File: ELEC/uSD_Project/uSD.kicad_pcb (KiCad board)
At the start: 2 copper layers, 70.6 x 25.3 mm, 18 parts, among them J1 CONN_01X08, J2 CONN_01X08, J3 CONN_02X04, J4 CONN_02X04, J5 CONN_01X08, J6 CONN_01X08, J7 CONN_01X20, U1 74HC595, U2 74HC165, U3 PADI_IoT_Stamp

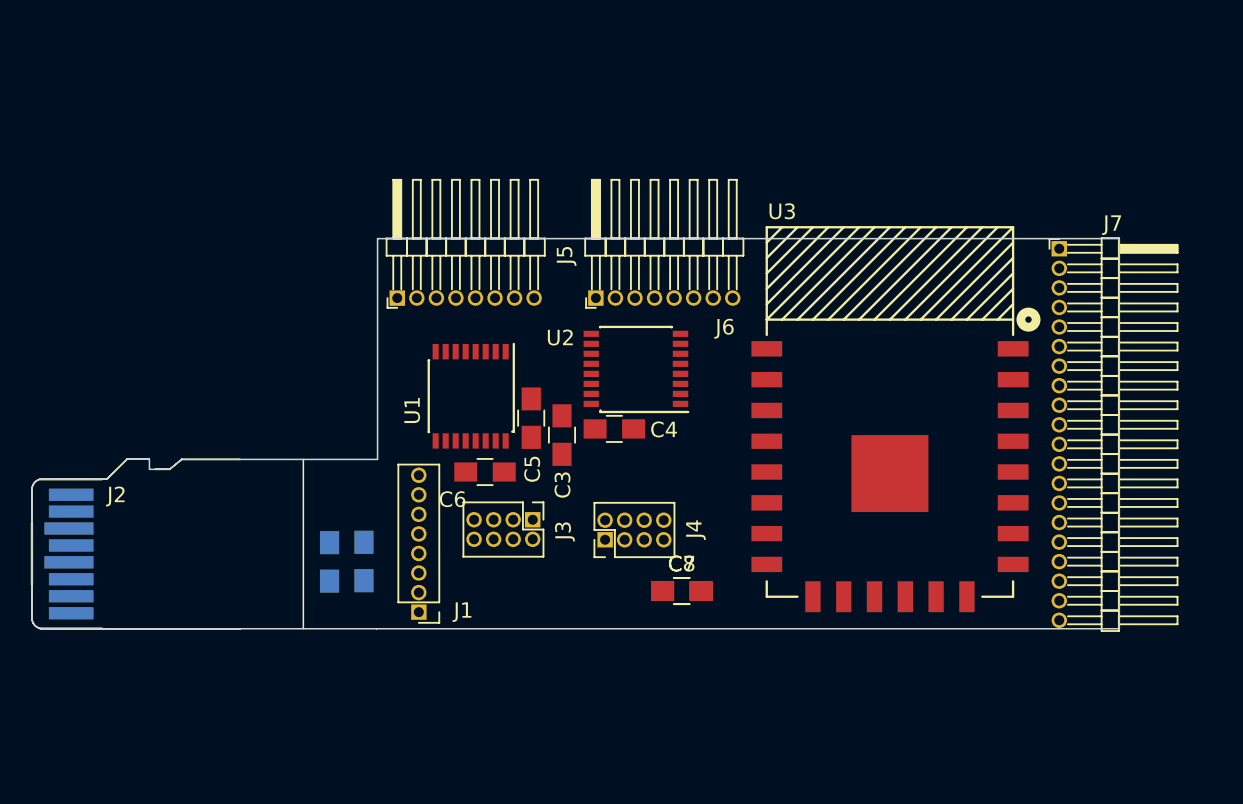
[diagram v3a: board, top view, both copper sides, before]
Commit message: Changed out shift registers, started and almost completed routing
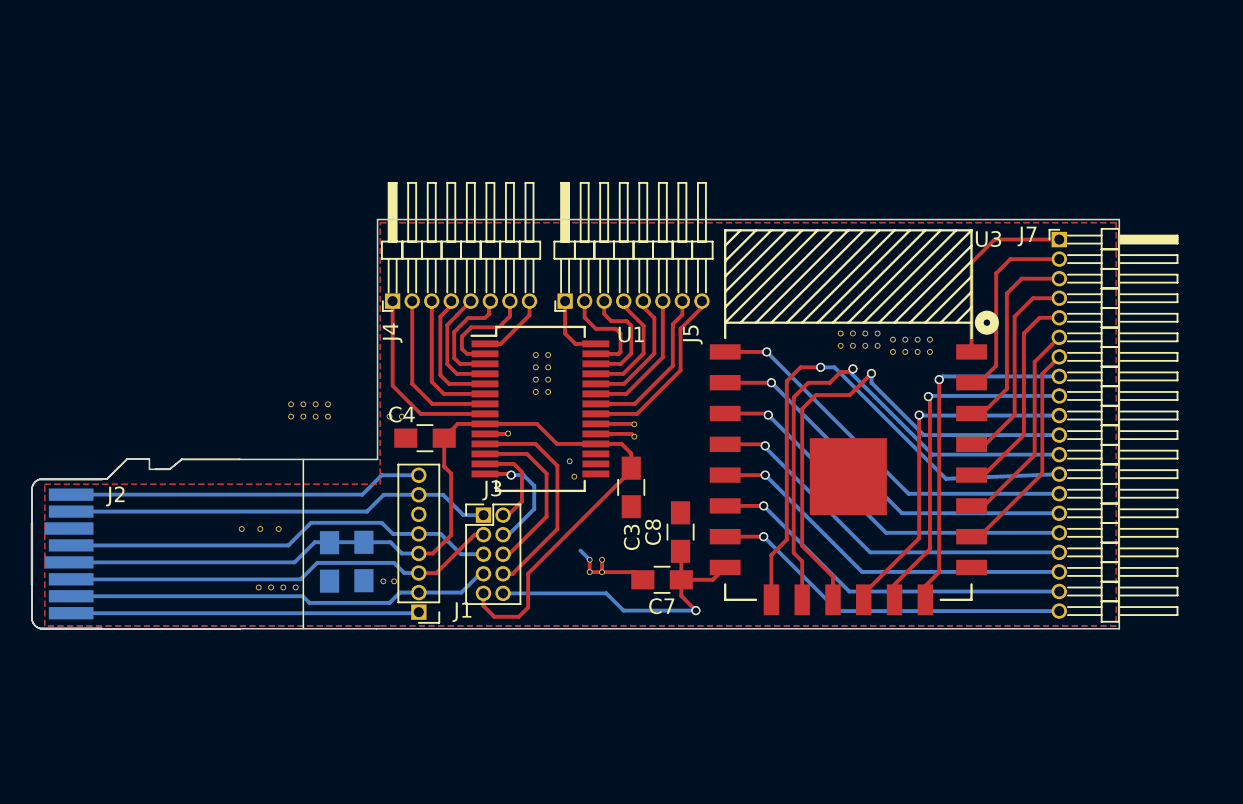
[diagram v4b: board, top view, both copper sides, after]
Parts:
- removed C5: 100nF, Capacitors_SMD:C_0805_HandSoldering
- removed C6: 1uF, Capacitors_SMD:C_0805_HandSoldering
- removed U2: 74HC165, Housings_SSOP.pretty:SSOP-16_4.4x5.2mm_Pitch0.65mm
- added J8: CONN_01X01, Via:10mil_Via, F.Cu at (153.5, 99.8)
- added REF**: Vias, Via:10mil_Via, F.Cu at (166.9, 93.9)
- added REF**: Vias, Via:10mil_Via, F.Cu at (171.1, 94.3)
- added REF**: Vias, Via:10mil_Via, F.Cu at (171.1, 95.1)
- added REF**: Vias, Via:10mil_Via, F.Cu at (170.3, 95.1)
- added REF**: Vias, Via:10mil_Via, F.Cu at (171.9, 95.1)
- added REF**: Vias, Via:10mil_Via, F.Cu at (172.7, 95.1)
- added REF**: Vias, Via:10mil_Via, F.Cu at (172.7, 94.3)
- added REF**: Vias, Via:10mil_Via, F.Cu at (171.9, 94.3)
- added REF**: Vias, Via:10mil_Via, F.Cu at (147.9, 95.3)
- added REF**: Vias, Via:10mil_Via, F.Cu at (147.9, 96.1)
- added REF**: Vias, Via:10mil_Via, F.Cu at (147.1, 96.1)
- added REF**: Vias, Via:10mil_Via, F.Cu at (167.7, 93.9)
- added REF**: Vias, Via:10mil_Via, F.Cu at (147.1, 95.3)
- added REF**: Vias, Via:10mil_Via, F.Cu at (147.1, 96.9)
- added REF**: Vias, Via:10mil_Via, F.Cu at (147.1, 97.7)
- added REF**: Vias, Via:10mil_Via, F.Cu at (147.9, 97.7)
- added REF**: Vias, Via:10mil_Via, F.Cu at (147.9, 96.9)
- added REF**: Vias, Via:10mil_Via, F.Cu at (132.8, 98.5)
- added REF**: Vias, Via:10mil_Via, F.Cu at (133.6, 98.5)
- added REF**: Vias, Via:10mil_Via, F.Cu at (133.6, 99.3)
- added REF**: Vias, Via:10mil_Via, F.Cu at (132.8, 99.3)
- added REF**: Vias, Via:10mil_Via, F.Cu at (131.2, 99.3)
- added REF**: Vias, Via:10mil_Via, F.Cu at (167.7, 94.7)
- added REF**: Vias, Via:10mil_Via, F.Cu at (132.0, 99.3)
- added REF**: Vias, Via:10mil_Via, F.Cu at (132.0, 98.5)
- added REF**: Vias, Via:10mil_Via, F.Cu at (131.2, 98.5)
- added REF**: Vias, Via:10mil_Via, F.Cu at (138.4, 99.3)
- added REF**: Vias, Via:10mil_Via, F.Cu at (137.6, 99.3)
- added REF**: Vias, Via:10mil_Via, F.Cu at (145.3, 100.4)
- added REF**: Vias, Via:10mil_Via, F.Cu at (149.3, 102.2)
- added REF**: Vias, Via:10mil_Via, F.Cu at (149.6, 103.2)
- added REF**: Vias, Via:10mil_Via, F.Cu at (137.2, 110.0)
- added REF**: Vias, Via:10mil_Via, F.Cu at (137.9, 110.0)
- added REF**: Vias, Via:10mil_Via, F.Cu at (166.9, 94.7)
- added REF**: Vias, Via:10mil_Via, F.Cu at (131.5, 110.4)
- added REF**: Vias, Via:10mil_Via, F.Cu at (130.7, 110.4)
- added REF**: Vias, Via:10mil_Via, F.Cu at (129.1, 110.4)
- added REF**: Vias, Via:10mil_Via, F.Cu at (129.9, 110.4)
- added REF**: Vias, Via:10mil_Via, F.Cu at (128.0, 106.6)
- added REF**: Vias, Via:10mil_Via, F.Cu at (129.2, 106.6)
- added REF**: Vias, Via:10mil_Via, F.Cu at (130.4, 106.6)
- added REF**: Vias, Via:10mil_Via, F.Cu at (151.4, 109.4)
- added REF**: Vias, Via:10mil_Via, F.Cu at (151.4, 108.6)
- added REF**: Vias, Via:10mil_Via, F.Cu at (150.6, 108.6)
- added REF**: Vias, Via:10mil_Via, F.Cu at (168.5, 94.7)
- added REF**: Vias, Via:10mil_Via, F.Cu at (150.6, 109.4)
- added REF**: Vias, Via:10mil_Via, F.Cu at (169.3, 94.7)
- added REF**: Vias, Via:10mil_Via, F.Cu at (169.3, 93.9)
- added REF**: Vias, Via:10mil_Via, F.Cu at (168.5, 93.9)
- added REF**: Vias, Via:10mil_Via, F.Cu at (170.3, 94.3)
- C3: value 100nF -> 1uF
- J3: value CONN_02X04 -> CONN_02X05; footprint Pin_Headers:Pin_Header_Straight_2x04_Pitch1.27mm -> Pin_Headers:Pin_Header_Straight_2x05_Pitch1.27mm
- J4: value CONN_02X04 -> CONN_01X08; footprint Pin_Headers:Pin_Header_Straight_2x04_Pitch1.27mm -> Pin_Headers:Pin_Header_Angled_1x08_Pitch1.27mm
- J6: value CONN_01X08 -> CONN_01X01; footprint Pin_Headers:Pin_Header_Angled_1x08_Pitch1.27mm -> Via:10mil_Via
- U1: value 74HC595 -> MCP23S17; footprint Housings_SSOP.pretty:SSOP-16_4.4x5.2mm_Pitch0.65mm -> Housings_SSOP.pretty:SSOP-28_5.3x10.2mm_Pitch0.65mm
- moved J4 20.8 mm to (137.8, 91.8)
- moved C4 12.3 mm to (139.9, 100.7), turned to 180 degrees
- moved J5 10.9 mm to (149.0, 91.8)
- moved J6 9.34 mm to (153.5, 100.6)
- moved C3 5.64 mm to (153.3, 103.9)
- moved U1 4.60 mm to (147.4, 98.8), turned to 0 degrees
- moved C8 3.83 mm to (156.5, 106.8), turned to 90 degrees
- moved J3 3.21 mm to (143.7, 105.7), turned to 0 degrees
- moved U3 2.71 mm to (159.4, 111.2)
- moved C7 1.48 mm to (155.3, 109.9), turned to 180 degrees
- moved J7 0.60 mm to (181.1, 87.8)
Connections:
- C1 pad 1: VCC -> VDD
- C2 pad 1: VCC -> VDD
- C3 pad 1: VCC -> VDD
- C4 pad 1: VCC -> VDD
- C7 pad 1: /Vdd_WIFI -> /Vdd_Wifi
- C8 pad 1: /Vdd_WIFI -> /Vdd_Wifi
- J1 pad 4: VCC -> VDD
- J2 pad 5: VCC -> VDD
- J3 pad 1: /595_Dat -> /DO
- J3 pad 2: /DO -> /MCP_DO
- J3 pad 3: /595_SRCLK -> /DI
- J3 pad 4: /CLK -> /MCP_DI
- J3 pad 5: /595_/OE -> /CLK
- J3 pad 6: /NC -> /MCP_CLK
- J3 pad 7: Net-(J3-Pad7) -> //CS
- J3 pad 8: Net-(J3-Pad8) -> /MCP_/CS
- J4 pad 1: /DI -> Net-(J4-Pad1)
- J4 pad 2: /165_Dat -> Net-(J4-Pad2)
- J4 pad 3: /CLK -> Net-(J4-Pad3)
- J4 pad 4: /165_CLK -> Net-(J4-Pad4)
- J4 pad 5: //CS -> Net-(J4-Pad5)
- J4 pad 6: /165_SHLD -> Net-(J4-Pad6)
- J4 pad 7: VCC -> Net-(J4-Pad7)
- J4 pad 8: /Vdd_WIFI -> Net-(J4-Pad8)
- J5 pad 1: /595_QH -> Net-(J5-Pad1)
- J5 pad 2: /595_QG -> Net-(J5-Pad2)
- J5 pad 3: /595_QF -> Net-(J5-Pad3)
- J5 pad 4: /595_QE -> Net-(J5-Pad4)
- J5 pad 5: /595_QD -> Net-(J5-Pad5)
- J5 pad 6: /595_QC -> Net-(J5-Pad6)
- J5 pad 7: /595_QB -> Net-(J5-Pad7)
- J5 pad 8: /595_QA -> Net-(J5-Pad8)
- J6 pad 1: /165_A -> Net-(J6-Pad1)
- J7 pad 14: /GE2 -> /GC2
- J7 pad 15: /GE3 -> /GC5
- J7 pad 16: /GE1 -> /CHIP-EN
- J7 pad 18: /CHIP-EN -> /GE1
- J7 pad 19: /GC5 -> /GE3
- J7 pad 20: /GC2 -> /GE2
- U1 pad 1: /595_QB -> Net-(J4-Pad8)
- U1 pad 10: VCC -> GND
- U1 pad 11: /595_SRCLK -> /MCP_/CS
- U1 pad 12: /595_/OE -> /MCP_CLK
- U1 pad 13: /595_/OE -> /MCP_DO
- U1 pad 14: /595_Dat -> /MCP_DI
- U1 pad 15: /595_QA -> GND
- U1 pad 16: VCC -> GND
- U1 pad 2: /595_QC -> Net-(J4-Pad7)
- U1 pad 3: /595_QD -> Net-(J4-Pad6)
- U1 pad 4: /595_QE -> Net-(J4-Pad5)
- U1 pad 5: /595_QF -> Net-(J4-Pad4)
- U1 pad 6: /595_QG -> Net-(J4-Pad3)
- U1 pad 7: /595_QH -> Net-(J4-Pad2)
- U1 pad 8: GND -> Net-(J4-Pad1)
- U1 pad 9: Net-(U1-Pad9) -> VDD
- U3 pad 15: /Vdd_WIFI -> /Vdd_Wifi
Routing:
- net VDD: track 0.00 -> 63.0 mm
- net /GA2: track 0.00 -> 35.7 mm, vias 0 -> 1
- net /GC4: track 0.00 -> 34.2 mm, vias 0 -> 1
- net /GA5: track 0.00 -> 33.4 mm, vias 0 -> 1
- net /DI: track 0.00 -> 28.5 mm
- net /CLK: track 0.00 -> 28.2 mm
- net /DO: track 0.00 -> 27.8 mm
- net //CS: track 0.00 -> 27.7 mm
- net /GC2: track 0.00 -> 25.5 mm, vias 0 -> 1
- net /GC5: track 0.00 -> 25.2 mm, vias 0 -> 1
- net /CHIP-EN: track 0.00 -> 25.1 mm, vias 0 -> 1
- net /GE4: track 0.00 -> 24.7 mm, vias 0 -> 1
- net /GE1: track 0.00 -> 24.3 mm, vias 0 -> 1
- net /GE3: track 0.00 -> 24.0 mm, vias 0 -> 1
- net /GE2: track 0.00 -> 23.7 mm, vias 0 -> 1
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- added copper zone on B.Cu, net GND
- added copper zone on F.Cu, net GND
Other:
- board size 70.6 x 25.3 mm -> 70.6 x 26.6 mm

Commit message: Finished layout, all the uSD pins are backwards. Last ECO
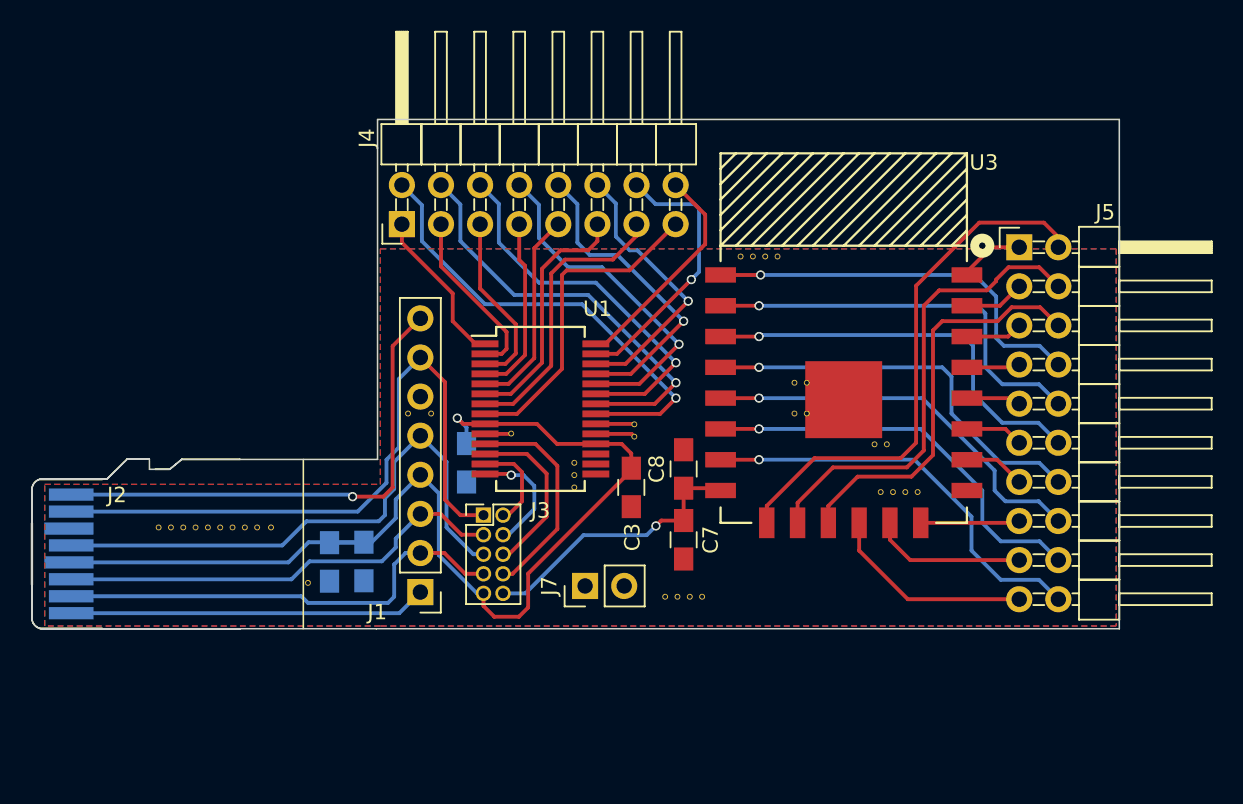
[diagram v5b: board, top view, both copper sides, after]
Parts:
- removed the REF** at (166.9, 93.9)
- removed the REF** at (171.1, 94.3)
- removed the REF** at (171.1, 95.1)
- removed the REF** at (170.3, 95.1)
- removed the REF** at (171.9, 95.1)
- removed the REF** at (172.7, 95.1)
- removed the REF** at (172.7, 94.3)
- removed the REF** at (171.9, 94.3)
- removed the REF** at (147.9, 95.3)
- removed the REF** at (147.9, 96.1)
- removed the REF** at (147.1, 96.1)
- removed the REF** at (167.7, 93.9)
- removed the REF** at (147.1, 95.3)
- removed the REF** at (147.1, 96.9)
- removed the REF** at (147.1, 97.7)
- removed the REF** at (147.9, 97.7)
- removed the REF** at (147.9, 96.9)
- removed the REF** at (132.8, 98.5)
- removed the REF** at (133.6, 98.5)
- removed the REF** at (133.6, 99.3)
- removed the REF** at (132.8, 99.3)
- removed the REF** at (131.2, 99.3)
- removed the REF** at (167.7, 94.7)
- removed the REF** at (132.0, 99.3)
- removed the REF** at (132.0, 98.5)
- removed the REF** at (131.2, 98.5)
- removed the REF** at (138.4, 99.3)
- removed the REF** at (137.6, 99.3)
- removed the REF** at (145.3, 100.4)
- removed the REF** at (149.3, 102.2)
- removed the REF** at (149.6, 103.2)
- removed the REF** at (137.2, 110.0)
- removed the REF** at (137.9, 110.0)
- removed the REF** at (166.9, 94.7)
- removed the REF** at (131.5, 110.4)
- removed the REF** at (130.7, 110.4)
- removed the REF** at (129.1, 110.4)
- removed the REF** at (129.9, 110.4)
- removed the REF** at (128.0, 106.6)
- removed the REF** at (129.2, 106.6)
- removed the REF** at (130.4, 106.6)
- removed the REF** at (151.4, 109.4)
- removed the REF** at (151.4, 108.6)
- removed the REF** at (150.6, 108.6)
- removed the REF** at (168.5, 94.7)
- removed the REF** at (150.6, 109.4)
- removed the REF** at (169.3, 94.7)
- removed the REF** at (169.3, 93.9)
- removed the REF** at (168.5, 93.9)
- removed the REF** at (170.3, 94.3)
- added REF**: Vias, Via:10mil_Via, F.Cu at (145.5, 100.4)
- added REF**: Vias, Via:10mil_Via, F.Cu at (160.4, 88.9)
- added REF**: Vias, Via:10mil_Via, F.Cu at (161.2, 88.9)
- added REF**: Vias, Via:10mil_Via, F.Cu at (162.0, 88.9)
- added REF**: Vias, Via:10mil_Via, F.Cu at (162.8, 88.9)
- added REF**: Vias, Via:10mil_Via, F.Cu at (169.1, 101.1)
- added REF**: Vias, Via:10mil_Via, F.Cu at (169.9, 101.1)
- added REF**: Vias, Via:10mil_Via, F.Cu at (163.9, 99.1)
- added REF**: Vias, Via:10mil_Via, F.Cu at (164.7, 99.1)
- added REF**: Vias, Via:10mil_Via, F.Cu at (163.9, 97.1)
- added REF**: Vias, Via:10mil_Via, F.Cu at (164.7, 97.1)
- added REF**: Vias, Via:10mil_Via, F.Cu at (155.5, 111.0)
- added REF**: Vias, Via:10mil_Via, F.Cu at (149.6, 103.9)
- added REF**: Vias, Via:10mil_Via, F.Cu at (149.6, 103.1)
- added REF**: Vias, Via:10mil_Via, F.Cu at (149.6, 102.3)
- added REF**: Vias, Via:10mil_Via, F.Cu at (124.2, 106.5)
- added REF**: Vias, Via:10mil_Via, F.Cu at (125.0, 106.5)
- added REF**: Vias, Via:10mil_Via, F.Cu at (123.4, 106.5)
- added REF**: Vias, Via:10mil_Via, F.Cu at (122.6, 106.5)
- added REF**: Vias, Via:10mil_Via, F.Cu at (125.8, 106.5)
- added REF**: Vias, Via:10mil_Via, F.Cu at (126.6, 106.5)
- added REF**: Vias, Via:10mil_Via, F.Cu at (128.2, 106.5)
- added REF**: Vias, Via:10mil_Via, F.Cu at (156.3, 111.0)
- added REF**: Vias, Via:10mil_Via, F.Cu at (127.4, 106.5)
- added REF**: Vias, Via:10mil_Via, F.Cu at (138.8, 99.1)
- added REF**: Vias, Via:10mil_Via, F.Cu at (132.3, 110.1)
- added REF**: Vias, Via:10mil_Via, F.Cu at (140.3, 99.1)
- added REF**: Vias, Via:10mil_Via, F.Cu at (129.0, 106.5)
- added REF**: Vias, Via:10mil_Via, F.Cu at (129.9, 106.5)
- added REF**: Vias, Via:10mil_Via, F.Cu at (157.1, 111.0)
- added REF**: Vias, Via:10mil_Via, F.Cu at (157.9, 111.0)
- added REF**: Vias, Via:10mil_Via, F.Cu at (171.1, 104.2)
- added REF**: Vias, Via:10mil_Via, F.Cu at (171.9, 104.2)
- added REF**: Vias, Via:10mil_Via, F.Cu at (169.5, 104.2)
- added REF**: Vias, Via:10mil_Via, F.Cu at (170.3, 104.2)
- C4: moved to B.Cu
- J1: footprint Pin_Headers:Pin_Header_Straight_1x08_Pitch1.27mm -> Pin_Headers:Pin_Header_Straight_1x08_Pitch2.54mm
- J4: value CONN_01X08 -> CONN_02X08; footprint Pin_Headers:Pin_Header_Angled_1x08_Pitch1.27mm -> Pin_Headers:Pin_Header_Angled_2x08_Pitch2.54mm
- J5: value CONN_01X08 -> CONN_02X10; footprint Pin_Headers:Pin_Header_Angled_1x08_Pitch1.27mm -> Pin_Headers:Pin_Header_Angled_2x10_Pitch2.54mm
- J7: value CONN_01X20 -> CONN_01X02; footprint Pin_Headers:Pin_Header_Angled_1x20_Pitch1.27mm -> Pin_Headers:Pin_Header_Straight_1x02_Pitch2.54mm
- moved J7 38.1 mm to (150.3, 110.3), turned to 90 degrees
- moved J5 29.7 mm to (178.5, 88.3), turned to 0 degrees
- moved J4 5.04 mm to (138.4, 86.8)
- moved U3 5.01 mm to (159.1, 106.2)
- moved C8 4.10 mm to (156.7, 102.7)
- moved C4 3.14 mm to (142.6, 102.3), turned to 270 degrees
- moved C7 2.95 mm to (156.7, 107.3), turned to 270 degrees
- moved J1 1.30 mm to (139.6, 110.7)
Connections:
- J4 pad 1: Net-(J4-Pad1) -> /GPB0
- J4 pad 3: Net-(J4-Pad3) -> /GPB1
- J4 pad 5: Net-(J4-Pad5) -> /GPB2
- J4 pad 7: Net-(J4-Pad7) -> /GPB3
- J5 pad 1: Net-(J5-Pad1) -> /GB0
- J5 pad 2: Net-(J5-Pad2) -> /GA5
- J5 pad 3: Net-(J5-Pad3) -> /GB1
- J5 pad 4: Net-(J5-Pad4) -> /GC4
- J5 pad 5: Net-(J5-Pad5) -> /GC1
- J5 pad 6: Net-(J5-Pad6) -> /GA2
- J5 pad 7: Net-(J5-Pad7) -> /GC3
- J5 pad 8: Net-(J5-Pad8) -> /GC2
- J7 pad 1: /GB0 -> GND
- J7 pad 2: /GB1 -> GND
- U1 pad 1: Net-(J4-Pad8) -> /GPB0
- U1 pad 2: Net-(J4-Pad7) -> /GPB1
- U1 pad 21: Net-(J5-Pad8) -> Net-(J4-Pad2)
- U1 pad 22: Net-(J5-Pad7) -> Net-(J4-Pad4)
- U1 pad 23: Net-(J5-Pad6) -> Net-(J4-Pad6)
- U1 pad 24: Net-(J5-Pad5) -> Net-(J4-Pad8)
- U1 pad 25: Net-(J5-Pad4) -> Net-(J4-Pad10)
- U1 pad 26: Net-(J5-Pad3) -> Net-(J4-Pad12)
- U1 pad 27: Net-(J5-Pad2) -> Net-(J4-Pad14)
- U1 pad 28: Net-(J5-Pad1) -> Net-(J4-Pad16)
- U1 pad 3: Net-(J4-Pad6) -> /GPB2
- U1 pad 4: Net-(J4-Pad5) -> /GPB3
- U1 pad 5: Net-(J4-Pad4) -> /GPB4
- U1 pad 6: Net-(J4-Pad3) -> /GPB5
- U1 pad 7: Net-(J4-Pad2) -> /GPB6
- U1 pad 8: Net-(J4-Pad1) -> /GPB7
- U3 pad 12: /GA5 -> /GA2
- U3 pad 14: /GA2 -> /GA5
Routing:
- net /GPB7: track 0.00 -> 21.1 mm
- net Net-(J4-Pad10): track 0.00 -> 20.4 mm, vias 0 -> 1
- net Net-(J4-Pad2): track 10.6 -> 30.5 mm, vias 0 -> 1
- net Net-(J4-Pad4): track 8.24 -> 27.7 mm, vias 0 -> 1
- net /GPB6: track 0.00 -> 18.6 mm
- net Net-(J4-Pad12): track 0.00 -> 18.0 mm, vias 0 -> 1
- net Net-(J4-Pad8): track 4.57 -> 22.4 mm, vias 0 -> 1
- net Net-(J4-Pad14): track 0.00 -> 17.7 mm, vias 0 -> 1
- net Net-(J4-Pad6): track 7.54 -> 25.0 mm, vias 0 -> 1
- net /GA3: track 22.6 -> 6.45 mm, vias 1 -> 0
- net /GPB5: track 0.00 -> 16.1 mm
- net /DO: track 27.8 -> 43.1 mm
- net Net-(J4-Pad16): track 0.00 -> 14.4 mm
- net /GPB4: track 0.00 -> 13.2 mm
- net /GA0: track 22.7 -> 10.0 mm, vias 1 -> 0
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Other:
- board size 70.6 x 26.6 mm -> 70.6 x 33.1 mm

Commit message: Flipped uSD connector so it's proper, generated gerbers, ordered PCBs!
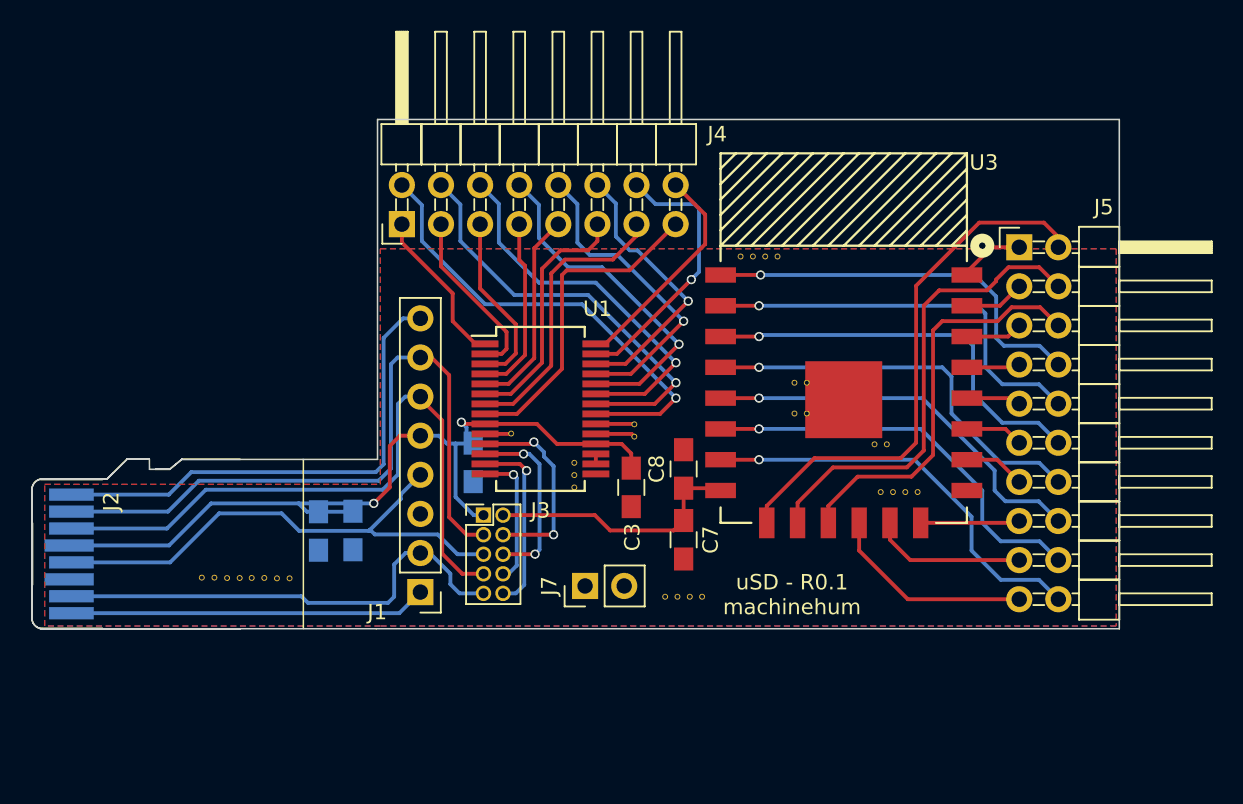
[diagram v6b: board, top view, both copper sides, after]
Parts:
- removed the REF** at (124.2, 106.5)
- removed the REF** at (125.0, 106.5)
- removed the REF** at (123.4, 106.5)
- removed the REF** at (122.6, 106.5)
- removed the REF** at (125.8, 106.5)
- removed the REF** at (126.6, 106.5)
- removed the REF** at (128.2, 106.5)
- removed the REF** at (127.4, 106.5)
- removed the REF** at (138.8, 99.1)
- removed the REF** at (140.3, 99.1)
- removed the REF** at (129.0, 106.5)
- removed the REF** at (129.9, 106.5)
- added REF**: Vias, Via:10mil_Via, F.Cu at (125.4, 109.8)
- added REF**: Vias, Via:10mil_Via, F.Cu at (126.2, 109.8)
- added REF**: Vias, Via:10mil_Via, F.Cu at (127.9, 109.8)
- added REF**: Vias, Via:10mil_Via, F.Cu at (127.0, 109.8)
- added REF**: Vias, Via:10mil_Via, F.Cu at (130.3, 109.8)
- added REF**: Vias, Via:10mil_Via, F.Cu at (131.1, 109.8)
- added REF**: Vias, Via:10mil_Via, F.Cu at (129.5, 109.8)
- moved REF** 3.67 mm to (128.6, 109.8)
- moved C2 2.14 mm to (135.2, 106.7)
- moved C1 2.14 mm to (133.0, 106.7)
- moved C4 0.43 mm to (143.0, 102.3)
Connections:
- J1 pad 1: /NC -> /RSV
- J1 pad 2: //CS -> /DO
- J1 pad 3: /DI -> GND
- J1 pad 4: VDD -> /CLK
- J1 pad 5: /CLK -> VDD
- J1 pad 6: GND -> /DI
- J1 pad 7: /DO -> //CS
- J1 pad 8: /RSV -> /NC
- J2 pad 1: /RSV -> /NC
- J2 pad 2: /DO -> //CS
- J2 pad 3: GND -> /DI
- J2 pad 4: /CLK -> VDD
- J2 pad 5: VDD -> /CLK
- J2 pad 6: /DI -> GND
- J2 pad 7: //CS -> /DO
- J2 pad 8: /NC -> /RSV
- J3 pad 1: /DO -> VDD
- J3 pad 10: /Vdd_Wifi -> /MCP_DO
- J3 pad 2: /MCP_DO -> /Vdd_Wifi
- J3 pad 3: /DI -> //CS
- J3 pad 4: /MCP_DI -> /MCP_/CS
- J3 pad 7: //CS -> /DI
- J3 pad 8: /MCP_/CS -> /MCP_DI
- J3 pad 9: VDD -> /DO
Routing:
- net //CS: track 30.1 -> 45.1 mm
- net VDD: track 69.0 -> 54.5 mm, vias 1 -> 2
- net /DI: track 29.4 -> 43.1 mm
- net /DO: track 43.1 -> 31.4 mm
- net /RSV: track 32.9 -> 23.2 mm, vias 1 -> 0
- net /NC: track 23.2 -> 32.2 mm
- net /MCP_DO: track 6.12 -> 12.0 mm, vias 0 -> 1
- net /CLK: track 37.1 -> 34.5 mm
- net /MCP_DI: track 7.74 -> 8.97 mm
- net /MCP_CLK: track 11.2 -> 12.3 mm, vias 0 -> 2
- net /MCP_/CS: track 14.1 -> 13.1 mm, vias 0 -> 2
- net /Vdd_Wifi: track 18.3 -> 17.3 mm, vias 1 -> 0
- net GND: track 1.71 -> 2.36 mm
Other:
- board text added: "uSD - R0.1 machinehum"
